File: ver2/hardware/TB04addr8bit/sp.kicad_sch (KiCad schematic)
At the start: 12 parts, among them U2 74AHC04, U35 74LS08, U36 74HC00, U37 74LS32, U38 74HC193, U5 74HC00

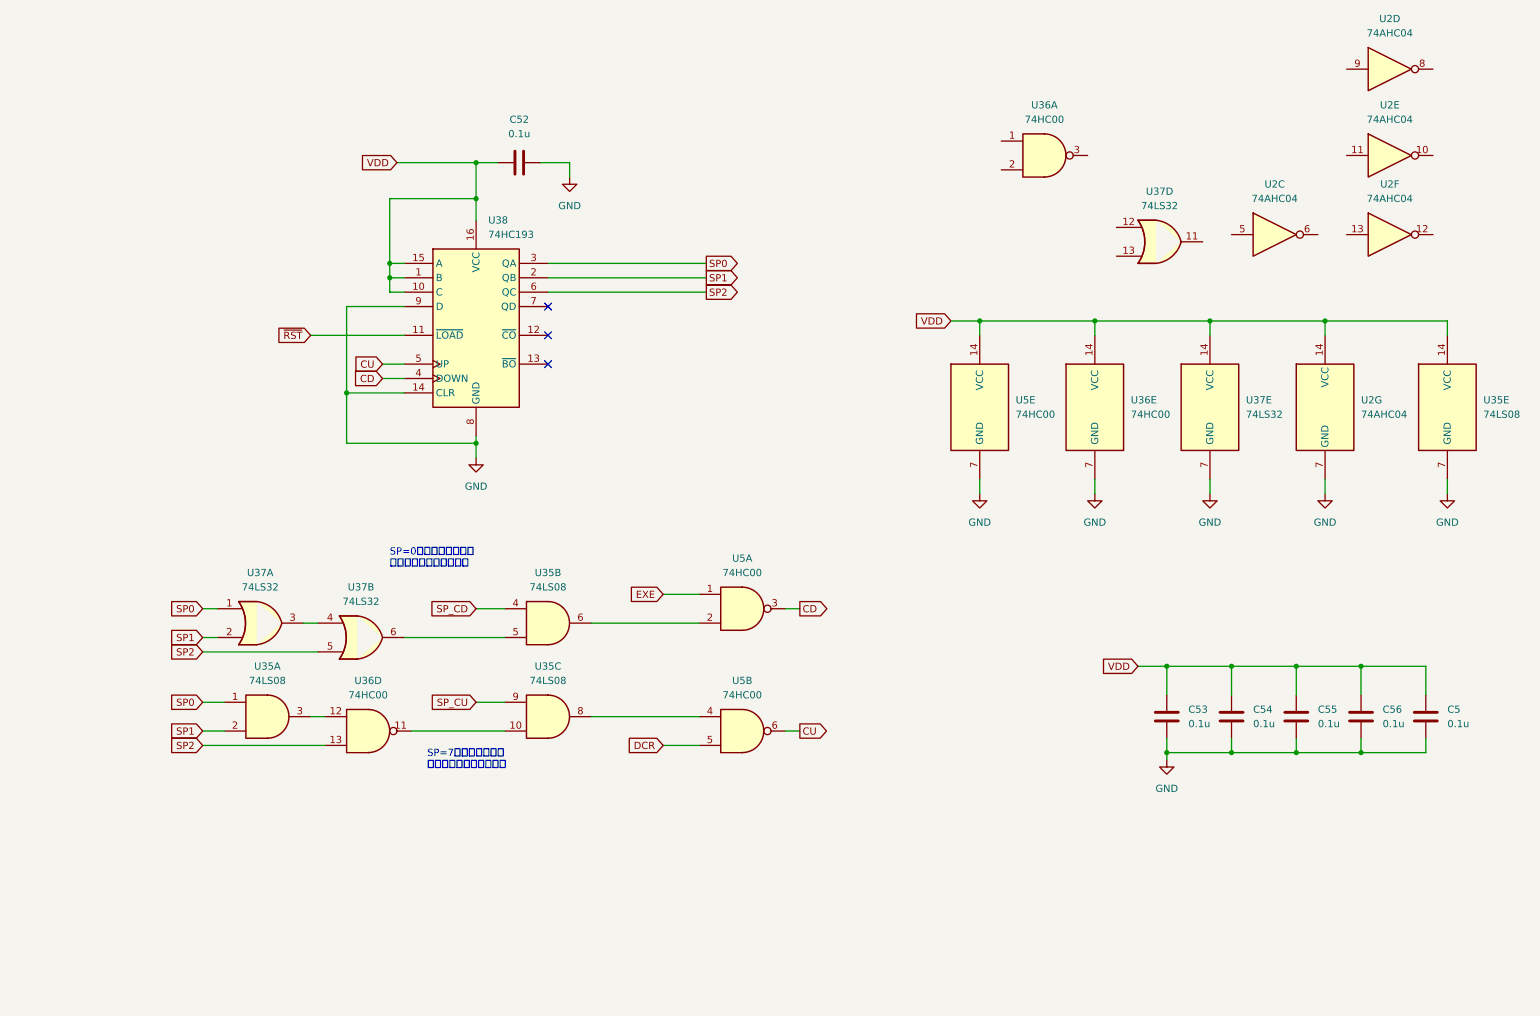
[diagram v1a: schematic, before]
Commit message: ver2: 要修正5件を修正し共通データバス・オペランド源MUX・I/Oを結線
- 6116の/CS極性を修正し、スタック域を含むRAM_STK_SEL(0xC0-0xF7)に統一
- ALU出力をDI0-3へ直結、U21はYドライバ源として残す(LD/POP/RET対策)
- 共通8bitデータバスMD0-7を新設(ROM/RAM/Yドライバ/IN244が排他駆動)
- aポートMUX(74LS253x2)・IN用244・Yドライバ制御ゲートを追加
- IN実行時のROM競合を/OE_ROMに~OE_iAddrを足して回避
- 4bit書込時にMD4-7が浮くのをU17 bank2で0駆動
- 74LS157のEをGND固定、孤立したPC_mAddrシートを削除

Co-Authored-By: Claude Opus 5 <noreply@anthropic.com>
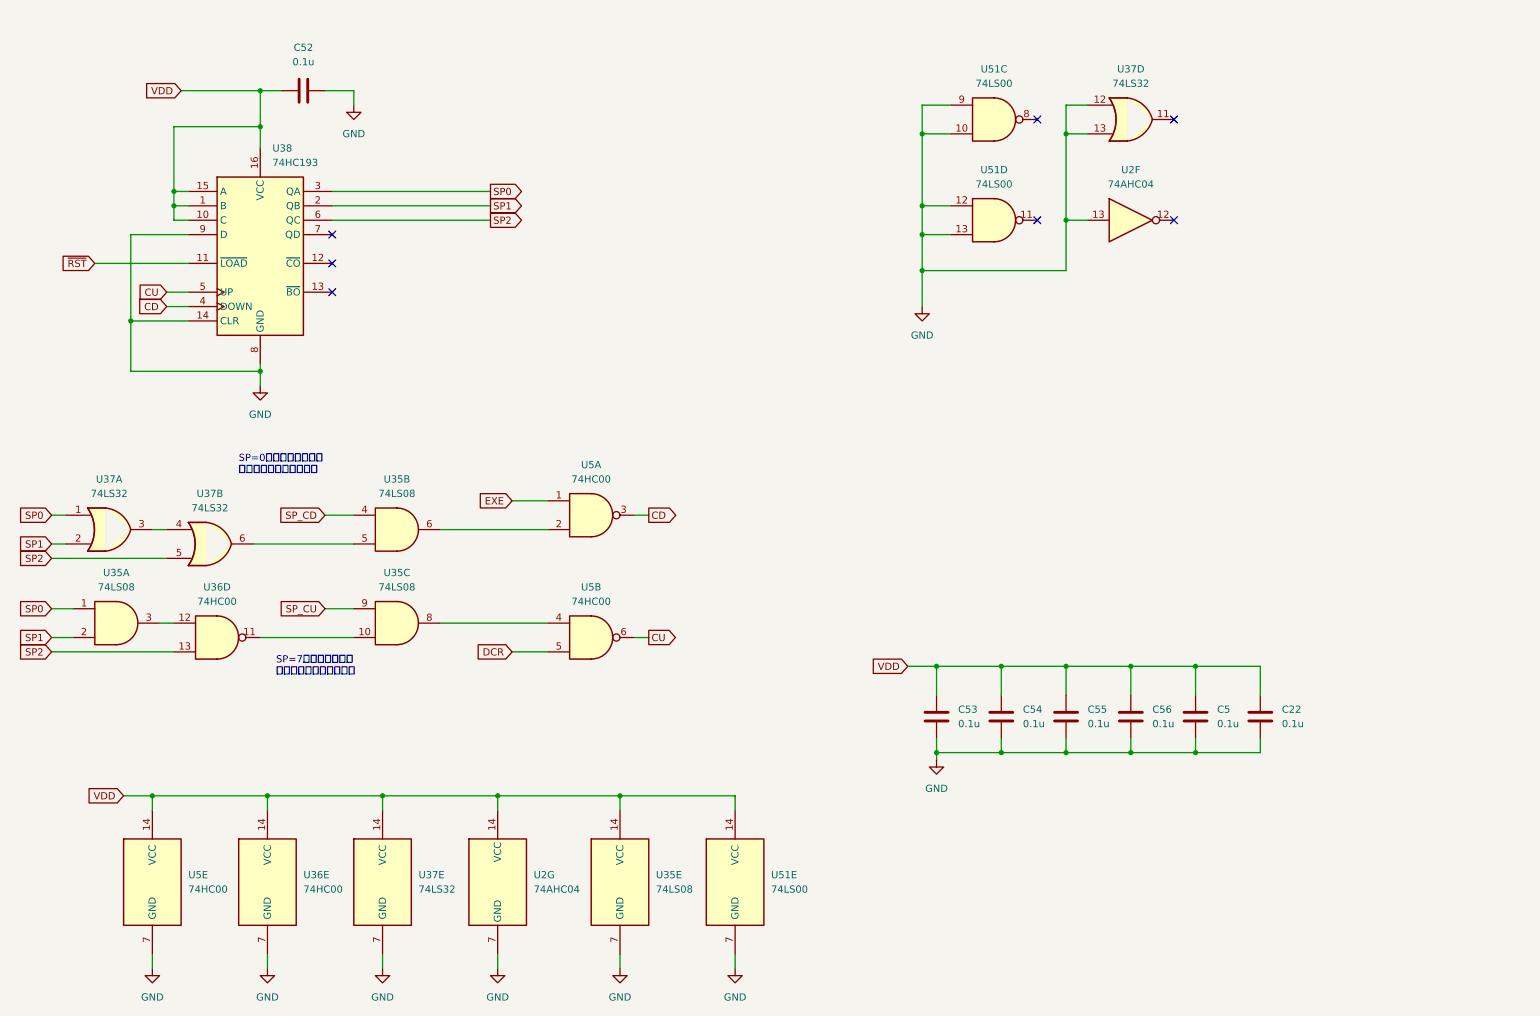
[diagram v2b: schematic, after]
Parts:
- removed unit 4 of U2
- removed unit 5 of U2
- removed unit 3 of U2
- removed unit 1 of U36
- added C22: 0.1u, Capacitor_THT:C_Disc_D4.3mm_W1.9mm_P5.00mm, symbol Device:C
- added U51: 74LS00, symbol 74xx:74LS00
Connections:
- net GND: now also U2.13, U37.12, U37.13, C22.2, U51.10, U51.12, U51.13, U51.7 (GND), U51.9
- net VDD: now also C22.1, U51.14 (VCC)
- no-connect marks 3 -> 7
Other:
- moved on the sheet: C5, C52, C53, C54, C55, C56, U2F, U2G, U35A, U35B, U35C, U35E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

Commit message: ver2: ゲートICをgatesシートへ集約しアノテーションを掛け直し
- 分散していた8パッケージ(U1/U2/U5/U25/U35/U36/U37/U51)をgatesシートへ集約
- シートをまたぐ11本をグローバルラベル化(~P4/~P5/~OUT_SEL/~CS_RAM/
  ~OE_ROM/CLK_C/CLK_Z/PC_CNT_EN/~PC_PE/~Ena_RS01/~Enb_RS01)
- U40のP2入力がROM_SELに吸着していたのを修正(RAM_SELが逆条件だった)
- !P5の重複インバータを解消、未使用ゲート入力7本をGNDへ
- ALU入力MUXをinPut→PC、PCカウンタをaddrMUX→PCへ移動
- 全体を再アノテーション(シート順採番)。旧→新の対応は電気的変化なしを確認

Co-Authored-By: Claude Opus 5 <noreply@anthropic.com>
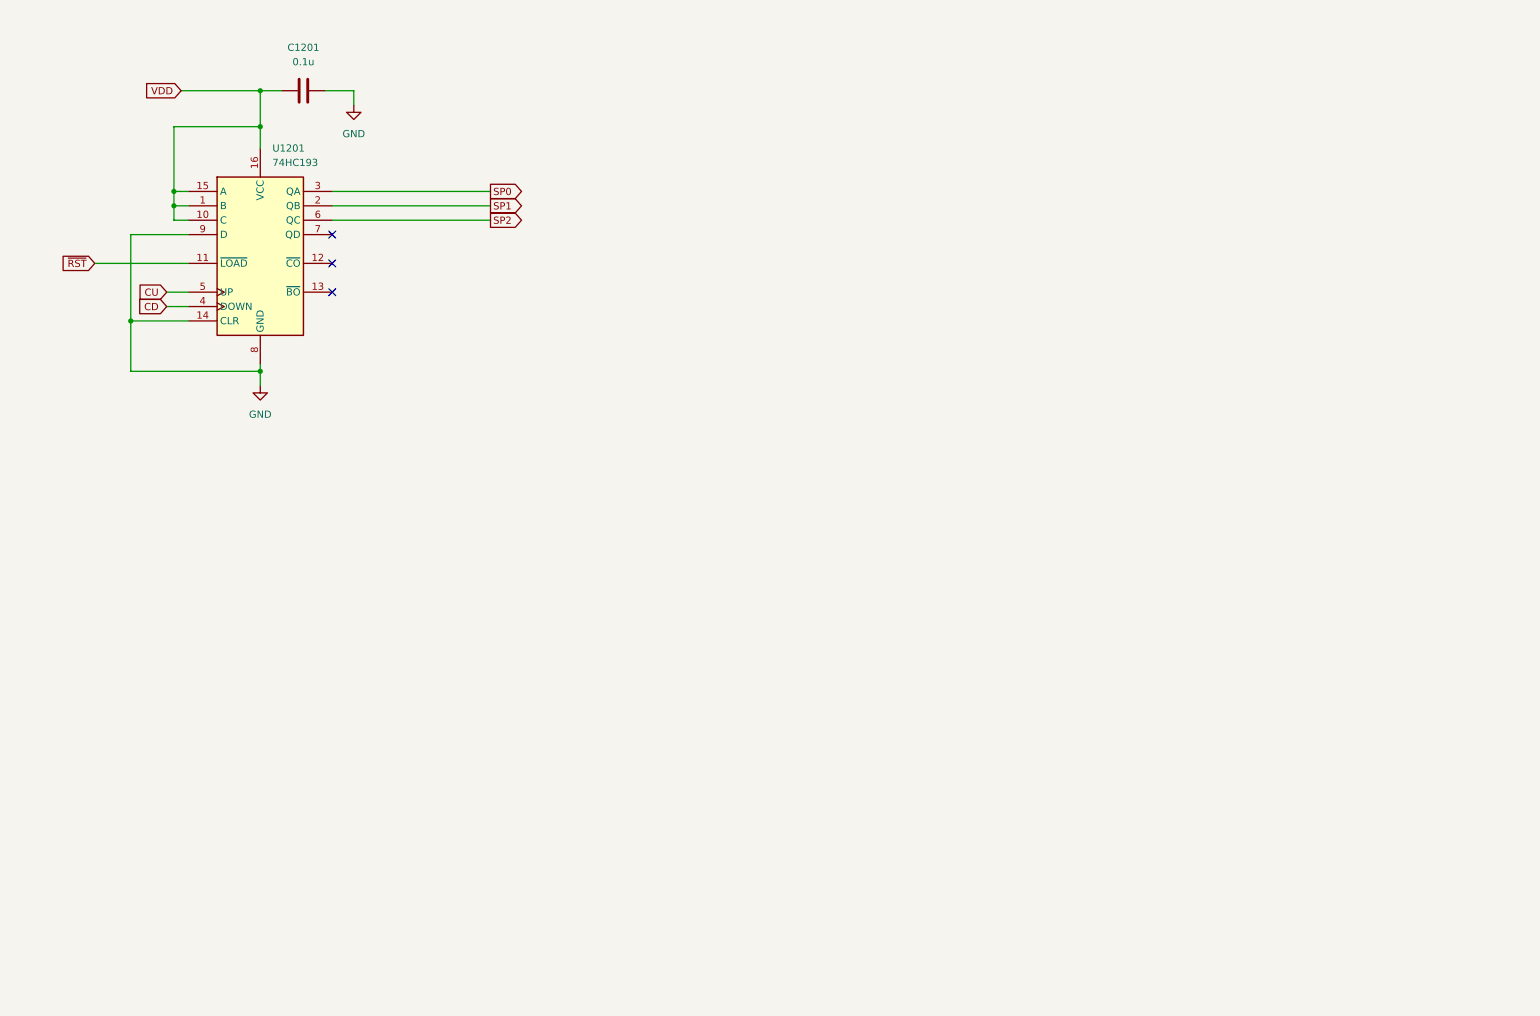
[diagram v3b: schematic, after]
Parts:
- removed C22, C5: 0.1u, Capacitor_THT:C_Disc_D4.3mm_W1.9mm_P5.00mm, symbol Device:C
- removed C53, C54, C55, C56: 0.1u, symbol Device:C
- removed U2: 74AHC04, symbol 74xx:74AHC04
- removed U35: 74LS08, symbol 74xx:74LS08
- removed U36, U5: 74HC00, symbol 74xx:74HC00
- removed U37: 74LS32, symbol 74xx:74LS32
- removed U51: 74LS00, symbol 74xx:74LS00
- renumbered C52 to C1201, U38 to U1201
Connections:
- no-connect marks 7 -> 3
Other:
- note removed: "SP=0のときそれ以下に カウントダウンさせない"
- note removed: "SP=7のときそれ以上 カウントアップさせない"
